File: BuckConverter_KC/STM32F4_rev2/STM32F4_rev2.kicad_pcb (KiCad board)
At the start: 4 copper layers, 50 parts, among them J1 Screw_Terminal_01x02, J2 SWD, J3 Conn_01x04, J4 Conn_01x04, J5 USB_B_Micro, Q1 AO3401A, SW1 SW_SPDT, U1 MP2359DJ-LF-Z, U2 STM32F405RGTy, U3 USBLC6-2SC6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

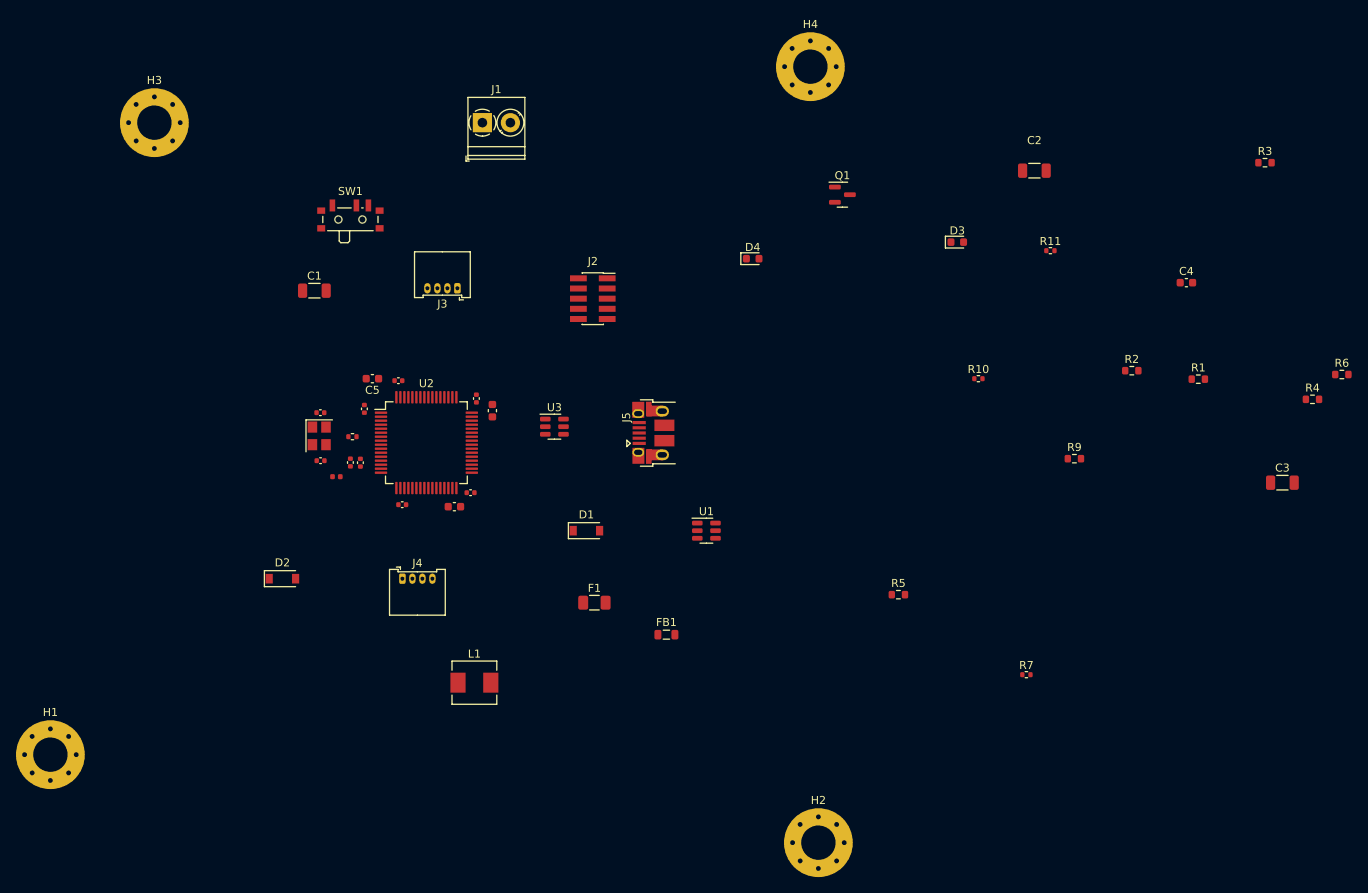
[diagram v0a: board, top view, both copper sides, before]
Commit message: finished layout less the 3v3 and gnd
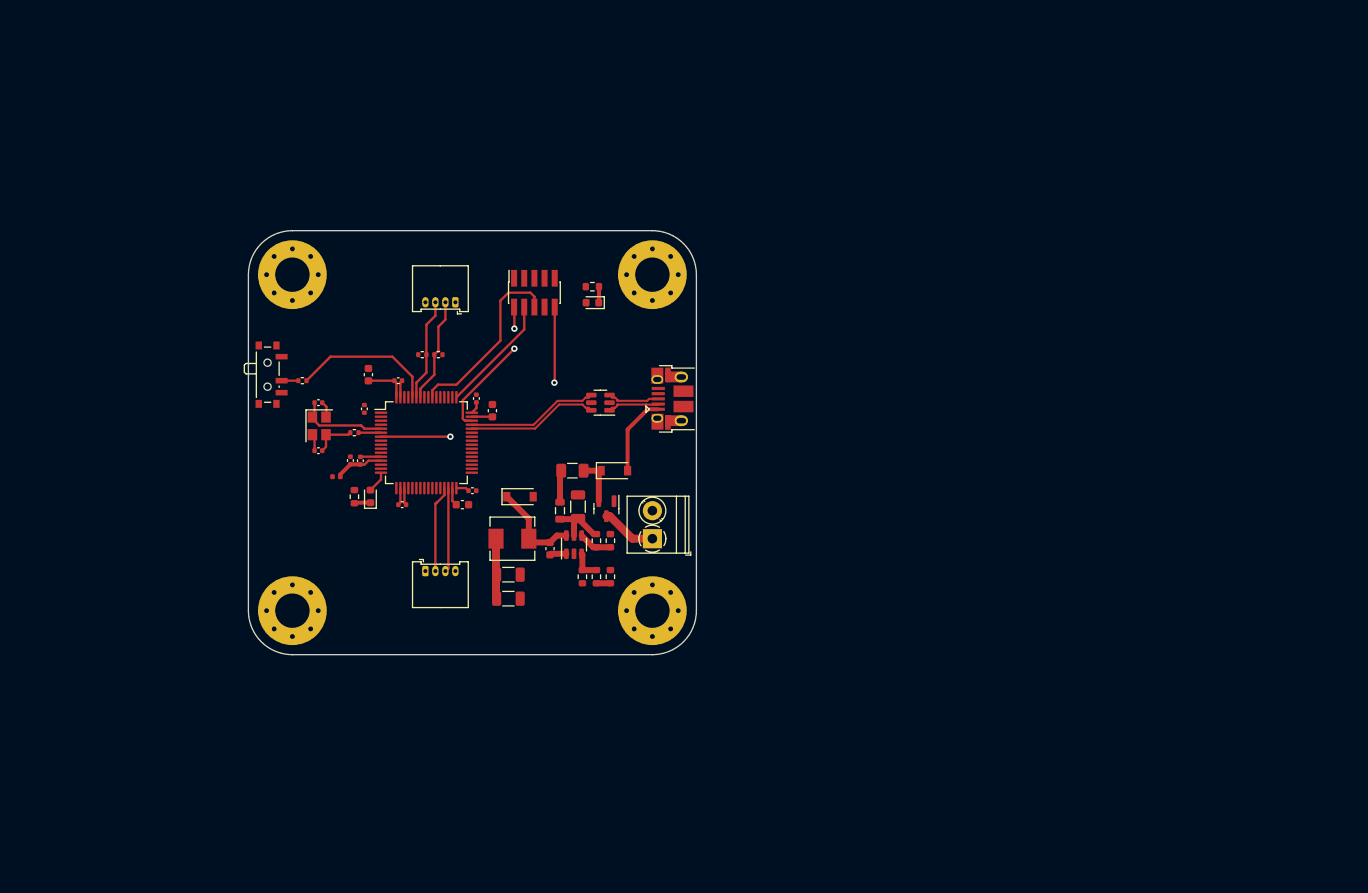
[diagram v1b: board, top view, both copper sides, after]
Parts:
- moved R3 99.8 mm to (106.5, 99.8), turned to 90 degrees
- moved C3 97.8 mm to (97.2, 102.5)
- moved R7 97.7 mm to (71.5, 75.2), turned to 180 degrees
- moved R6 94.3 mm to (107.8, 63.5), turned to 180 degrees
- moved R4 92.2 mm to (108.2, 99.8), turned to -90 degrees
- moved R9 90.1 mm to (78.0, 89.8), turned to 90 degrees
- moved C4 86.2 mm to (102.5, 96.2), turned to -90 degrees
- moved C2 82.9 mm to (97.2, 99.5)
- moved R11 79.6 mm to (86.5, 72.0)
- moved R1 77.9 mm to (108.2, 95.2), turned to -90 degrees
- moved R2 68.6 mm to (110.0, 95.2), turned to 90 degrees
- moved R10 67.6 mm to (88.5, 72.0), turned to 180 degrees
- moved D4 56.3 mm to (80.0, 89.7), turned to 90 degrees
- moved J1 56.2 mm to (115.2, 95.0), turned to 90 degrees
- moved Q1 49.1 mm to (109.5, 91.2), turned to -90 degrees
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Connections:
- net USB__CONN_D- renamed USB_CONN_D-
- D1 pad 1: Net-(Q1-Pad2) -> Net-(D1-Pad1)
- F1 pad 1: +12V -> Net-(D1-Pad1)
- F1 pad 2: Net-(F1-Pad2) -> Net-(FB1-Pad1)
- FB1 pad 1: Net-(Q1-Pad2) -> Net-(FB1-Pad1)
- Q1 pad 2: Net-(Q1-Pad2) -> Net-(D1-Pad1)
- Q1 pad 3: Net-(F1-Pad2) -> +12V
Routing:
- net NRST: track 0.00 -> 33.9 mm, vias 0 -> 2
- net SWO: track 0.00 -> 23.1 mm
- net +3.3V: track 0.00 -> 18.4 mm
- net BOOT0: track 0.00 -> 18.1 mm
- net SWDIO: track 0.00 -> 17.9 mm, vias 0 -> 2
- net USB_D-: track 0.00 -> 16.5 mm
- net USB_D+: track 0.00 -> 16.5 mm
- net SWCLK: track 0.00 -> 14.8 mm
- net I2C1_SCL: track 0.00 -> 13.2 mm
- net I2C1_SDA: track 0.00 -> 12.9 mm
- net BUCK_SW: track 0.00 -> 11.6 mm
- net HSE_IN: track 0.00 -> 11.2 mm
- net GND: track 0.00 -> 11.1 mm
- net USART3_TX: track 0.00 -> 10.9 mm
- net USART3_RX: track 0.00 -> 10.5 mm
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- added copper zone on In2.Cu, net +3.3V
- added copper zone on In1.Cu, net GND
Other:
- board outline added: 56 x 53 mm

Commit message: finished layout; generated gerber, component footprints position files, BOM
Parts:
- J2: footprint Connector_PinSocket_1.27mm:PinSocket_2x05_P1.27mm_Vertical_SMD -> Connector_PinHeader_1.27mm:PinHeader_2x05_P1.27mm_Vertical_SMD
- moved R7 1.06 mm to (72.2, 74.5)
- moved SW1 1.06 mm to (68.2, 73.8)
- turned J2 to -90 degrees
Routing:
- net GND: track 11.1 -> 83.9 mm, vias 0 -> 35
- net +3.3V: track 18.4 -> 36.3 mm, vias 0 -> 13
- net unconnected-(J5-Pad6): track 0.00 -> 11.8 mm
- net +5V: track 10.0 -> 16.3 mm
- net NRST: track 33.9 -> 27.7 mm
- net SWO: track 23.1 -> 18.5 mm
- net SWDIO: track 17.9 -> 22.4 mm, vias 2 -> 0
- net SWCLK: track 14.8 -> 16.4 mm
- net BOOT0: track 18.1 -> 17.3 mm
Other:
- board text added: "3V3"
- board text added: "BOOT"
- board text added: "I2C"
- board text added: "POWER"
- board text added: "STATUS"
- board text added: "SWD"
- board text added: "UART"
- board text added: "USB"

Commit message: updating BuckConverter project
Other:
- board text added: "RUN"
- board text added: "STM32F4 TEST BOARD | REV 2"
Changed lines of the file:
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@@
       (usegerberattributes true)
       (usegerberadvancedattributes true)
-      (creategerberjobfile true)
+      (creategerberjobfile false)
       (svguseinch false)
       (svgprecision 6)
@@
       (outputformat 1)
       (mirror false)
-      (drillshape 1)
+      (drillshape 0)
       (scaleselection 1)
-      (outputdirectory "")
+      (outputdirectory "gerber/")
     )
   )
@@
     (fp_line (start -1.6 -0.8) (end 1.6 -0.8) (layer "F.Fab") (width 0.1))
     (fp_line (start 1.6 0.8) (end -1.6 0.8) (layer "F.Fab") (width 0.1))
-    (pad "1" smd roundrect (at -1.475 0) (size 1.15 1.8) (layers "F.Cu" "F.Paste" "F.Mask") (roundrect_rratio 0.217391)
+    (pad "1" smd roundrect (at -1.475 0) (size 1.15 1.8) (layers "F.Cu" "F.Paste" "F.Mask") (roundrect_rratio 0.2173913043)
       (net 7 "+3.3V") (pintype "passive"))
-    (pad "2" smd roundrect (at 1.475 0) (size 1.15 1.8) (layers "F.Cu" "F.Paste" "F.Mask") (roundrect_rratio 0.217391)
+    (pad "2" smd roundrect (at 1.475 0) (size 1.15 1.8) (layers "F.Cu" "F.Paste" "F.Mask") (roundrect_rratio 0.2173913043)
       (net 76 "GND") (pintype "passive"))
     (model "${KICAD6_3DMODEL_DIR}/Capacitor_SMD.3dshapes/C_1206_3216Metric.wrl"
@@
     (fp_line (start 1.6 -0.8) (end 1.6 0.8) (layer "F.Fab") (width 0.1))
     (fp_line (start -1.6 0.8) (end -1.6 -0.8) (layer "F.Fab") (width 0.1))
-    (pad "1" smd roundrect (at -1.475 0 90) (size 1.15 1.8) (layers "F.Cu" "F.Paste" "F.Mask") (roundrect_rratio 0.217391)
+    (pad "1" smd roundrect (at -1.475 0 90) (size 1.15 1.8) (layers "F.Cu" "F.Paste" "F.Mask") (roundrect_rratio 0.2173913043)
       (net 9 "BUCK_IN") (pintype "passive"))
-    (pad "2" smd roundrect (at 1.475 0 90) (size 1.15 1.8) (layers "F.Cu" "F.Paste" "F.Mask") (roundrect_rratio 0.217391)
+    (pad "2" smd roundrect (at 1.475 0 90) (size 1.15 1.8) (layers "F.Cu" "F.Paste" "F.Mask") (roundrect_rratio 0.2173913043)
       (net 76 "GND") (pintype "passive"))
     (model "${KICAD6_3DMODEL_DIR}/Capacitor_SMD.3dshapes/C_1206_3216Metric.wrl"
@@
     (fp_line (start 1.6 -0.8) (end 1.6 0.8) (layer "F.Fab") (width 0.1))
     (fp_line (start 1.6 0.8) (end -1.6 0.8) (layer "F.Fab") (width 0.1))
-    (pad "1" smd roundrect (at -1.475 0) (size 1.15 1.8) (layers "F.Cu" "F.Paste" "F.Mask") (roundrect_rratio 0.217391)
+    (pad "1" smd roundrect (at -1.475 0) (size 1.15 1.8) (layers "F.Cu" "F.Paste" "F.Mask") (roundrect_rratio 0.2173913043)
       (net 7 "+3.3V") (pintype "passive"))
-    (pad "2" smd roundrect (at 1.475 0) (size 1.15 1.8) (layers "F.Cu" "F.Paste" "F.Mask") (roundrect_rratio 0.217391)
+    (pad "2" smd roundrect (at 1.475 0) (size 1.15 1.8) (layers "F.Cu" "F.Paste" "F.Mask") (roundrect_rratio 0.2173913043)
       (net 76 "GND") (pintype "passive"))
     (model "${KICAD6_3DMODEL_DIR}/Capacitor_SMD.3dshapes/C_1206_3216Metric.wrl"
@@
     )
   )
+  (gr_circle (center 102.9716 60.4266) (end 103.1494 60.2742) (layer "F.SilkS") (width 0.15) (fill none))
+  (gr_circle (center 100.2284 91.6178) (end 100.3808 91.7448) (layer "F.SilkS") (width 0.15) (fill none))
+  (gr_line (start 115.316 97.917) (end 115.316 97.1042) (layer "F.SilkS") (width 0.15))
+  (gr_line (start 114.8588 97.5106) (end 115.7732 97.5106) (layer "F.SilkS") (width 0.15))
+  (gr_circle (center 80.01 79.2226) (end 80.0608 79.1972) (layer "F.SilkS") (width 0.15) (fill none))
+  (gr_circle (center 71.4756 70.7898) (end 71.4248 70.612) (layer "F.SilkS") (width 0.15) (fill none))
+  (gr_circle (center 90.8812 67.4878) (end 90.805 67.2084) (layer "F.SilkS") (width 0.15) (fill none))
+  (gr_circle (center 86.995 97.0788) (end 87.122 97.2312) (layer "F.SilkS") (width 0.15) (fill none))
   (gr_line (start 115.25 109.5) (end 70.25 109.5) (layer "Edge.Cuts") (width 0.1))
   (gr_arc (start 115.25 56.5) (mid 119.139087 58.110913) (end 120.75 62) (layer "Edge.Cuts") (width 0.1))
@@
     (effects (font (size 1 1) (thickness 0.15)))
   )
+  (gr_text "STM32F4 TEST BOARD | REV 2" (at 97.3328 107.442) (layer "F.SilkS")
+    (effects (font (size 1 1) (thickness 0.15)))
+  )
   (gr_text "USB" (at 118 83) (layer "F.SilkS")
     (effects (font (size 1 1) (thickness 0.15)))
@@
     (effects (font (size 1 1) (thickness 0.15)))
   )
-  (gr_text "BOOT" (at 73.25 70) (layer "F.SilkS")
+  (gr_text "BOOT" (at 68.5292 68.4022) (layer "F.SilkS")
     (effects (font (size 1 1) (thickness 0.15)))
   )
+  (gr_text "RUN" (at 68.4784 79.4766) (layer "F.SilkS")
+    (effects (font (size 1 1) (thickness 0.15)))
+  )
